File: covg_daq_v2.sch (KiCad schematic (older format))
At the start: 4 parts

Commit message: updates to README
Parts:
- added J?: HDMI_A, symbol Connector:HDMI_A
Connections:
- net labels added: GND
- wire segments 0 -> 12
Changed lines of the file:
@@
 L adc_dac_v1-eagle-import:MOUNT-HOLE3.0 H1
 U 1 1 60986F3F
-P 7450 7850
+P 9650 7550
 AR Path="/60986F3F" Ref="H1"  Part="1"
 AR Path="/6095A004/60986F3F" Ref="H?"  Part="1"
-F 0 "H1" H 7530 7873 59  0000 L BNN
-F 1 "MOUNT-HOLE3.0" H 7530 7753 59  0000 L BNN
-F 2 "adc_dac_v1:3,0" H 7450 7850 50  0001 C CNN
-F 3 "" H 7450 7850 50  0001 C CNN
-	1    7450 7850
+F 0 "H1" H 9730 7573 59  0000 L BNN
+F 1 "MOUNT-HOLE3.0" H 9730 7453 59  0000 L BNN
+F 2 "adc_dac_v1:3,0" H 9650 7550 50  0001 C CNN
+F 3 "" H 9650 7550 50  0001 C CNN
+	1    9650 7550
 	1    0    0    -1
 $EndComp
@@
 L adc_dac_v1-eagle-import:MOUNT-HOLE3.0 H2
 U 1 1 60986F45
-P 8550 7850
+P 10750 7550
 AR Path="/60986F45" Ref="H2"  Part="1"
 AR Path="/6095A004/60986F45" Ref="H?"  Part="1"
-F 0 "H2" H 8630 7873 59  0000 L BNN
-F 1 "MOUNT-HOLE3.0" H 8630 7753 59  0000 L BNN
-F 2 "adc_dac_v1:3,0" H 8550 7850 50  0001 C CNN
-F 3 "" H 8550 7850 50  0001 C CNN
-	1    8550 7850
+F 0 "H2" H 10830 7573 59  0000 L BNN
+F 1 "MOUNT-HOLE3.0" H 10830 7453 59  0000 L BNN
+F 2 "adc_dac_v1:3,0" H 10750 7550 50  0001 C CNN
+F 3 "" H 10750 7550 50  0001 C CNN
+	1    10750 7550
 	1    0    0    -1
 $EndComp
@@
 	1    0    0    -1
 $EndComp
+$Comp
+L Connector:HDMI_A J?
+U 1 1 61D74FD2
+P 1150 6550
+F 0 "J?" H 1580 6596 50  0000 L CNN
+F 1 "HDMI_A" H 1580 6505 50  0000 L CNN
+F 2 "" H 1175 6550 50  0001 C CNN
+F 3 "https://en.wikipedia.org/wiki/HDMI" H 1175 6550 50  0001 C CNN
+	1    1150 6550
+	-1   0    0    -1
+$EndComp
+$Comp
+L power:GND #PWR?
+U 1 1 61D76AA5
+P 700 7850
+F 0 "#PWR?" H 700 7600 50  0001 C CNN
+F 1 "GND" H 705 7677 50  0001 C CNN
+F 2 "" H 700 7850 50  0001 C CNN
+F 3 "" H 700 7850 50  0001 C CNN
+	1    700  7850
+	1    0    0    -1
+$EndComp
+Wire Wire Line
+	700  7850 850  7850
+Wire Wire Line
+	850  7850 850  7650
+Wire Wire Line
+	850  7850 950  7850
+Wire Wire Line
+	1350 7850 1350 7650
+Connection ~ 850  7850
+Wire Wire Line
+	1250 7650 1250 7850
+Connection ~ 1250 7850
+Wire Wire Line
+	1250 7850 1350 7850
+Wire Wire Line
+	1150 7850 1150 7650
+Connection ~ 1150 7850
+Wire Wire Line
+	1150 7850 1250 7850
+Wire Wire Line
+	1050 7650 1050 7850
+Connection ~ 1050 7850
+Wire Wire Line
+	1050 7850 1150 7850
+Wire Wire Line
+	950  7850 950  7650
+Connection ~ 950  7850
+Wire Wire Line
+	950  7850 1050 7850
 $EndSCHEMATC

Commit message: updates to fast adc schematic
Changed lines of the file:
@@
 $EndDescr
 $Sheet
-S 1000 1000 500  150
+S 8900 3600 500  150
 U 6095A004
 F0 "gp_adc" 50
@@
 $EndSheet
 $Sheet
-S 5000 1000 500  150
+S 7150 2200 500  150
 U 6095A38A
 F0 "level_shifters" 50
@@
 $EndSheet
 $Sheet
-S 7000 1000 500  150
+S 1400 4350 500  150
 U 6095A697
 F0 "adc1" 50
@@
 $EndSheet
 $Sheet
-S 5000 3000 500  150
+S 2450 4350 500  150
 U 6095B316
 F0 "dac1" 50
@@
 $EndSheet
 $Sheet
-S 3000 5000 500  150
+S 8900 950  500  150
 U 6095BD4C
 F0 "dac_gp" 50
@@
 $EndSheet
 $Sheet
-S 5000 5000 500  150
+S 8900 2300 500  150
 U 6095BE10
 F0 "power" 50
@@
 $EndSheet
 $Sheet
-S 3000 1000 500  150
+S 7200 900  500  150
 U 6095A302
 F0 "ok_fpga" 50

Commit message: completed fast ADC and DAC; start on gp DAC
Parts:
- removed H1, H2, H3, H4: MOUNT-HOLE3.0, adc_dac_v1:3,0, symbol adc_dac_v1-eagle-import:MOUNT-HOLE3.0
- added H? (x4): MountingHole_Pad, MountingHole:MountingHole_3.2mm_M3_DIN965_Pad, symbol Mechanical:MountingHole_Pad
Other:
- moved on the sheet: J?
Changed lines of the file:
@@
 $EndDescr
-$Sheet
-S 8900 3600 500  150
-U 6095A004
-F0 "gp_adc" 50
-F1 "gp_adc.sch" 50
-$EndSheet
 $Sheet
 S 7150 2200 500  150
@@
 F0 "level_shifters" 50
 F1 "level_shifters.sch" 50
-$EndSheet
-$Sheet
-S 1400 4350 500  150
-U 6095A697
-F0 "adc1" 50
-F1 "adc1.sch" 50
-$EndSheet
-$Sheet
-S 2450 4350 500  150
-U 6095B316
-F0 "dac1" 50
-F1 "dac1.sch" 50
 $EndSheet
 $Sheet
@@
 $EndSheet
 $Comp
-L adc_dac_v1-eagle-import:FRAME_A_L #FRAME2
-U 1 1 60986F39
-P 7050 8150
-AR Path="/60986F39" Ref="#FRAME2"  Part="1"
-AR Path="/6095A004/60986F39" Ref="#FRAME?"  Part="1"
-F 0 "#FRAME2" H 7050 8150 50  0001 C CNN
-F 1 "FRAME_A_L" H 7050 8150 50  0001 C CNN
-F 2 "" H 7050 8150 50  0001 C CNN
-F 3 "" H 7050 8150 50  0001 C CNN
-	1    7050 8150
+L Connector:HDMI_A J?
+U 1 1 61D74FD2
+P 2000 5950
+F 0 "J?" H 2430 5996 50  0000 L CNN
+F 1 "HDMI_A" H 2430 5905 50  0000 L CNN
+F 2 "" H 2025 5950 50  0001 C CNN
+F 3 "https://en.wikipedia.org/wiki/HDMI" H 2025 5950 50  0001 C CNN
+	1    2000 5950
+	0    -1   1    0
+$EndComp
+$Comp
+L power:GND #PWR0101
+U 1 1 61D76AA5
+P 3300 6400
+F 0 "#PWR0101" H 3300 6150 50  0001 C CNN
+F 1 "GND" H 3305 6227 50  0001 C CNN
+F 2 "" H 3300 6400 50  0001 C CNN
+F 3 "" H 3300 6400 50  0001 C CNN
+	1    3300 6400
+	0    -1   -1   0
+$EndComp
+Wire Wire Line
+	3300 6400 3300 6250
+Wire Wire Line
+	3300 6250 3100 6250
+Wire Wire Line
+	3300 6250 3300 6150
+Wire Wire Line
+	3300 5750 3100 5750
+Connection ~ 3300 6250
+Wire Wire Line
+	3100 5850 3300 5850
+Connection ~ 3300 5850
+Wire Wire Line
+	3300 5850 3300 5750
+Wire Wire Line
+	3300 5950 3100 5950
+Connection ~ 3300 5950
+Wire Wire Line
+	3300 5950 3300 5850
+Wire Wire Line
+	3100 6050 3300 6050
+Connection ~ 3300 6050
+Wire Wire Line
+	3300 6050 3300 5950
+Wire Wire Line
+	3300 6150 3100 6150
+Connection ~ 3300 6150
+Wire Wire Line
+	3300 6150 3300 6050
+$Sheet
+S 1000 3900 1050 950
+U 6095A697
+F0 "adc" 50
+F1 "adc.sch" 50
+F2 "CNV_P" I R 2050 3950 50
+F3 "CNV_N" I R 2050 4050 50
+F4 "D_N" O R 2050 4150 50
+F5 "DCO_N" O R 2050 4250 50
+F6 "DCO_P" O R 2050 4350 50
+F7 "CLK_N" I R 2050 4450 50
+F8 "CLK_P" I R 2050 4550 50
+F9 "VCM_OUT" O L 1000 4650 50
+F10 "IN_N" I L 1000 4200 50
+F11 "IN_P" I L 1000 4100 50
+F12 "A_EN0" I R 2050 4750 50
+$EndSheet
+$Sheet
+S 2850 3900 650  350
+U 6095B316
+F0 "dac" 50
+F1 "dac.sch" 50
+F2 "CSB" I L 2850 3950 50
+F3 "SCLK" I L 2850 4050 50
+F4 "SDI" I L 2850 4150 50
+F5 "OUT" O R 3500 4000 50
+$EndSheet
+$Comp
+L Mechanical:MountingHole_Pad H?
+U 1 1 60B0A4A6
+P 1700 750
+F 0 "H?" H 1800 799 50  0000 L CNN
+F 1 "MountingHole_Pad" H 1800 708 50  0000 L CNN
+F 2 "MountingHole:MountingHole_3.2mm_M3_DIN965_Pad" H 1700 750 50  0001 C CNN
+F 3 "~" H 1700 750 50  0001 C CNN
+	1    1700 750
 	1    0    0    -1
 $EndComp
 $Comp
-L adc_dac_v1-eagle-import:MOUNT-HOLE3.0 H1
-U 1 1 60986F3F
-P 9650 7550
-AR Path="/60986F3F" Ref="H1"  Part="1"
-AR Path="/6095A004/60986F3F" Ref="H?"  Part="1"
-F 0 "H1" H 9730 7573 59  0000 L BNN
-F 1 "MOUNT-HOLE3.0" H 9730 7453 59  0000 L BNN
-F 2 "adc_dac_v1:3,0" H 9650 7550 50  0001 C CNN
-F 3 "" H 9650 7550 50  0001 C CNN
-	1    9650 7550
+L Mechanical:MountingHole_Pad H?
+U 1 1 60B0AC43
+P 700 750
+F 0 "H?" H 800 799 50  0000 L CNN
+F 1 "MountingHole_Pad" H 800 708 50  0000 L CNN
+F 2 "MountingHole:MountingHole_3.2mm_M3_DIN965_Pad" H 700 750 50  0001 C CNN
+F 3 "~" H 700 750 50  0001 C CNN
+	1    700  750
 	1    0    0    -1
 $EndComp
 $Comp
-L adc_dac_v1-eagle-import:MOUNT-HOLE3.0 H2
-U 1 1 60986F45
-P 10750 7550
-AR Path="/60986F45" Ref="H2"  Part="1"
-AR Path="/6095A004/60986F45" Ref="H?"  Part="1"
-F 0 "H2" H 10830 7573 59  0000 L BNN
-F 1 "MOUNT-HOLE3.0" H 10830 7453 59  0000 L BNN
-F 2 "adc_dac_v1:3,0" H 10750 7550 50  0001 C CNN
-F 3 "" H 10750 7550 50  0001 C CNN
-	1    10750 7550
+L Mechanical:MountingHole_Pad H?
+U 1 1 60B0ADFD
+P 700 1200
+F 0 "H?" H 800 1249 50  0000 L CNN
+F 1 "MountingHole_Pad" H 800 1158 50  0000 L CNN
+F 2 "MountingHole:MountingHole_3.2mm_M3_DIN965_Pad" H 700 1200 50  0001 C CNN
+F 3 "~" H 700 1200 50  0001 C CNN
+	1    700  1200
 	1    0    0    -1
 $EndComp
 $Comp
-L adc_dac_v1-eagle-import:MOUNT-HOLE3.0 H3
-U 1 1 60986F4B
-P 9650 7850
-AR Path="/60986F4B" Ref="H3"  Part="1"
-AR Path="/6095A004/60986F4B" Ref="H?"  Part="1"
-F 0 "H3" H 9730 7873 59  0000 L BNN
-F 1 "MOUNT-HOLE3.0" H 9730 7753 59  0000 L BNN
-F 2 "adc_dac_v1:3,0" H 9650 7850 50  0001 C CNN
-F 3 "" H 9650 7850 50  0001 C CNN
-	1    9650 7850
+L Mechanical:MountingHole_Pad H?
+U 1 1 60B0B098
+P 1700 1200
+F 0 "H?" H 1800 1249 50  0000 L CNN
+F 1 "MountingHole_Pad" H 1800 1158 50  0000 L CNN
+F 2 "MountingHole:MountingHole_3.2mm_M3_DIN965_Pad" H 1700 1200 50  0001 C CNN
+F 3 "~" H 1700 1200 50  0001 C CNN
+	1    1700 1200
 	1    0    0    -1
 $EndComp
-$Comp
-L adc_dac_v1-eagle-import:MOUNT-HOLE3.0 H4
-U 1 1 60986F51
-P 10750 7850
-AR Path="/60986F51" Ref="H4"  Part="1"
-AR Path="/6095A004/60986F51" Ref="H?"  Part="1"
-F 0 "H4" H 10830 7873 59  0000 L BNN
-F 1 "MOUNT-HOLE3.0" H 10830 7753 59  0000 L BNN
-F 2 "adc_dac_v1:3,0" H 10750 7850 50  0001 C CNN
-F 3 "" H 10750 7850 50  0001 C CNN
-	1    10750 7850
-	1    0    0    -1
-$EndComp
-$Comp
-L Connector:HDMI_A J?
-U 1 1 61D74FD2
-P 1150 6550
-F 0 "J?" H 1580 6596 50  0000 L CNN
-F 1 "HDMI_A" H 1580 6505 50  0000 L CNN
-F 2 "" H 1175 6550 50  0001 C CNN
-F 3 "https://en.wikipedia.org/wiki/HDMI" H 1175 6550 50  0001 C CNN
-	1    1150 6550
-	-1   0    0    -1
-$EndComp
-$Comp
-L power:GND #PWR?
-U 1 1 61D76AA5
-P 700 7850
-F 0 "#PWR?" H 700 7600 50  0001 C CNN
-F 1 "GND" H 705 7677 50  0001 C CNN
-F 2 "" H 700 7850 50  0001 C CNN
-F 3 "" H 700 7850 50  0001 C CNN
-	1    700  7850
-	1    0    0    -1
-$EndComp
-Wire Wire Line
-	700  7850 850  7850
-Wire Wire Line
-	850  7850 850  7650
-Wire Wire Line
-	850  7850 950  7850
-Wire Wire Line
-	1350 7850 1350 7650
-Connection ~ 850  7850
-Wire Wire Line
-	1250 7650 1250 7850
-Connection ~ 1250 7850
-Wire Wire Line
-	1250 7850 1350 7850
-Wire Wire Line
-	1150 7850 1150 7650
-Connection ~ 1150 7850
-Wire Wire Line
-	1150 7850 1250 7850
-Wire Wire Line
-	1050 7650 1050 7850
-Connection ~ 1050 7850
-Wire Wire Line
-	1050 7850 1150 7850
-Wire Wire Line
-	950  7850 950  7650
-Connection ~ 950  7850
-Wire Wire Line
-	950  7850 1050 7850
+$Sheet
+S 8900 3600 500  150
+U 6095A004
+F0 "adc_gp" 50
+F1 "adc_gp.sch" 50
+$EndSheet
 $EndSCHEMATC

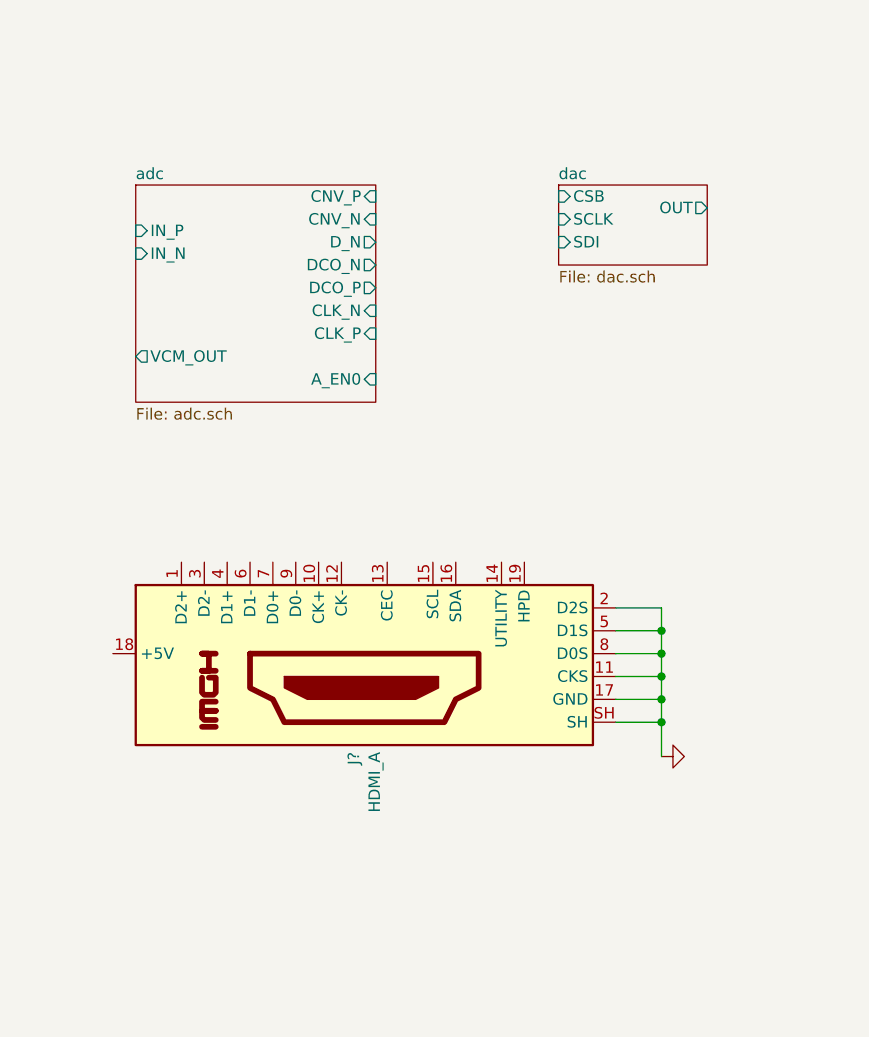
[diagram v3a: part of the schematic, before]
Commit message: updates to the gp DAC
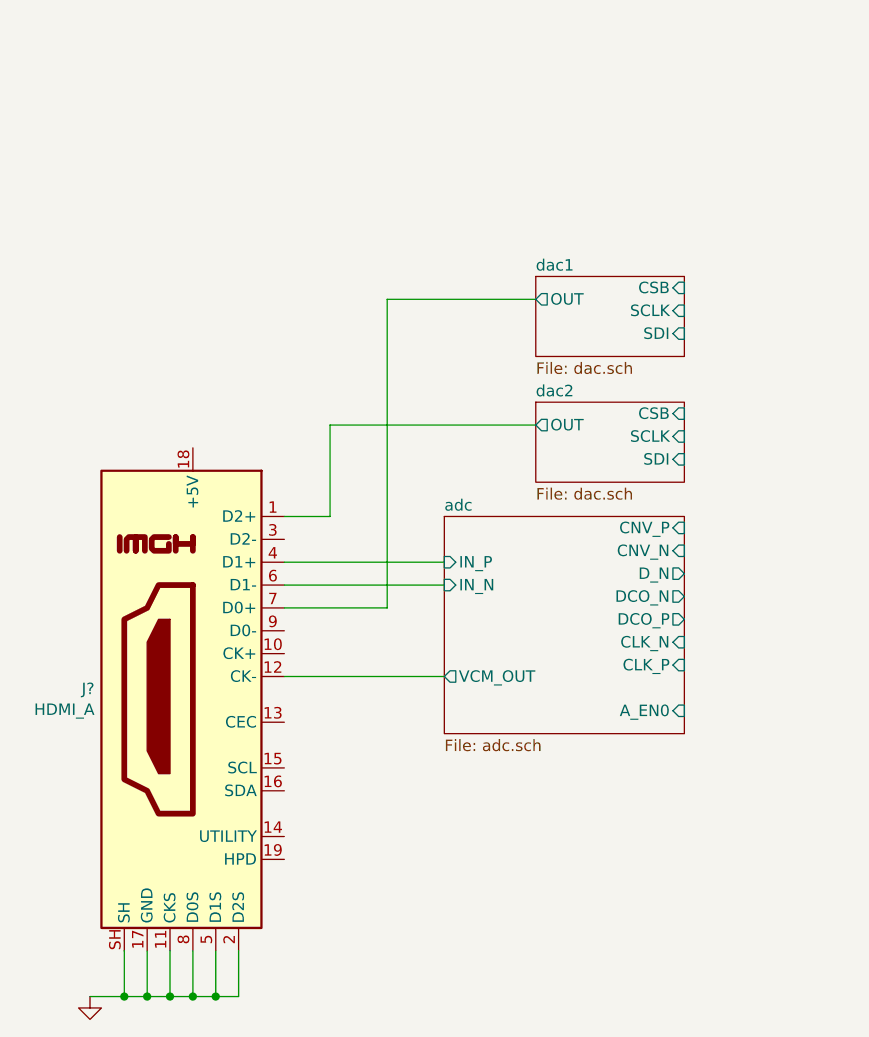
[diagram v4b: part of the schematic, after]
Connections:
- net adc/IN_N: now also J?.6 (D1-)
- net adc/IN_P: now also J?.4 (D1+)
- net adc/VCM_OUT: now also J?.12 (CK-)
- net dac2/OUT: now reaches J?.1 (D2+)
- net dac1/OUT: now reaches J?.7 (D0+)
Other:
- moved on the sheet: J?
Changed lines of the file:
@@
 $Descr A4 11693 8268
 encoding utf-8
-Sheet 1 8
+Sheet 1 9
 Title ""
 Date ""
@@
 L Connector:HDMI_A J?
 U 1 1 61D74FD2
-P 2000 5950
-F 0 "J?" H 2430 5996 50  0000 L CNN
-F 1 "HDMI_A" H 2430 5905 50  0000 L CNN
-F 2 "" H 2025 5950 50  0001 C CNN
-F 3 "https://en.wikipedia.org/wiki/HDMI" H 2025 5950 50  0001 C CNN
-	1    2000 5950
-	0    -1   1    0
+P 1250 6150
+F 0 "J?" H 1680 6196 50  0000 L CNN
+F 1 "HDMI_A" H 1680 6105 50  0000 L CNN
+F 2 "" H 1275 6150 50  0001 C CNN
+F 3 "https://en.wikipedia.org/wiki/HDMI" H 1275 6150 50  0001 C CNN
+	1    1250 6150
+	-1   0    0    -1
 $EndComp
 $Comp
 L power:GND #PWR0101
 U 1 1 61D76AA5
-P 3300 6400
-F 0 "#PWR0101" H 3300 6150 50  0001 C CNN
-F 1 "GND" H 3305 6227 50  0001 C CNN
-F 2 "" H 3300 6400 50  0001 C CNN
-F 3 "" H 3300 6400 50  0001 C CNN
-	1    3300 6400
-	0    -1   -1   0
+P 800 7450
+F 0 "#PWR0101" H 800 7200 50  0001 C CNN
+F 1 "GND" H 805 7277 50  0001 C CNN
+F 2 "" H 800 7450 50  0001 C CNN
+F 3 "" H 800 7450 50  0001 C CNN
+	1    800  7450
+	1    0    0    -1
 $EndComp
 Wire Wire Line
-	3300 6400 3300 6250
+	800  7450 950  7450
 Wire Wire Line
-	3300 6250 3100 6250
+	950  7450 950  7250
 Wire Wire Line
-	3300 6250 3300 6150
+	950  7450 1050 7450
 Wire Wire Line
-	3300 5750 3100 5750
-Connection ~ 3300 6250
+	1450 7450 1450 7250
+Connection ~ 950  7450
 Wire Wire Line
-	3100 5850 3300 5850
-Connection ~ 3300 5850
+	1350 7250 1350 7450
+Connection ~ 1350 7450
 Wire Wire Line
-	3300 5850 3300 5750
+	1350 7450 1450 7450
 Wire Wire Line
-	3300 5950 3100 5950
-Connection ~ 3300 5950
+	1250 7450 1250 7250
+Connection ~ 1250 7450
 Wire Wire Line
-	3300 5950 3300 5850
+	1250 7450 1350 7450
 Wire Wire Line
-	3100 6050 3300 6050
-Connection ~ 3300 6050
+	1150 7250 1150 7450
+Connection ~ 1150 7450
 Wire Wire Line
-	3300 6050 3300 5950
+	1150 7450 1250 7450
 Wire Wire Line
-	3300 6150 3100 6150
-Connection ~ 3300 6150
+	1050 7450 1050 7250
+Connection ~ 1050 7450
 Wire Wire Line
-	3300 6150 3300 6050
+	1050 7450 1150 7450
 $Sheet
-S 1000 3900 1050 950
+S 2350 5350 1050 950
 U 6095A697
 F0 "adc" 50
 F1 "adc.sch" 50
-F2 "CNV_P" I R 2050 3950 50
-F3 "CNV_N" I R 2050 4050 50
-F4 "D_N" O R 2050 4150 50
-F5 "DCO_N" O R 2050 4250 50
-F6 "DCO_P" O R 2050 4350 50
-F7 "CLK_N" I R 2050 4450 50
-F8 "CLK_P" I R 2050 4550 50
-F9 "VCM_OUT" O L 1000 4650 50
-F10 "IN_N" I L 1000 4200 50
-F11 "IN_P" I L 1000 4100 50
-F12 "A_EN0" I R 2050 4750 50
+F2 "CNV_P" I R 3400 5400 50
+F3 "CNV_N" I R 3400 5500 50
+F4 "D_N" O R 3400 5600 50
+F5 "DCO_N" O R 3400 5700 50
+F6 "DCO_P" O R 3400 5800 50
+F7 "CLK_N" I R 3400 5900 50
+F8 "CLK_P" I R 3400 6000 50
+F9 "VCM_OUT" O L 2350 6050 50
+F10 "IN_N" I L 2350 5650 50
+F11 "IN_P" I L 2350 5550 50
+F12 "A_EN0" I R 3400 6200 50
 $EndSheet
 $Sheet
-S 2850 3900 650  350
+S 2750 4300 650  350
 U 6095B316
-F0 "dac" 50
+F0 "dac1" 50
 F1 "dac.sch" 50
-F2 "CSB" I L 2850 3950 50
-F3 "SCLK" I L 2850 4050 50
-F4 "SDI" I L 2850 4150 50
-F5 "OUT" O R 3500 4000 50
+F2 "CSB" I R 3400 4350 50
+F3 "SCLK" I R 3400 4450 50
+F4 "SDI" I R 3400 4550 50
+F5 "OUT" O L 2750 4400 50
 $EndSheet
 $Comp
@@
 F1 "adc_gp.sch" 50
 $EndSheet
+Wire Wire Line
+	1650 5550 2350 5550
+Wire Wire Line
+	2350 5650 1650 5650
+Wire Wire Line
+	2350 6050 1650 6050
+$Sheet
+S 2750 4850 650  350
+U 60BDA97E
+F0 "dac2" 50
+F1 "dac.sch" 50
+F2 "CSB" I R 3400 4900 50
+F3 "SCLK" I R 3400 5000 50
+F4 "SDI" I R 3400 5100 50
+F5 "OUT" O L 2750 4950 50
+$EndSheet
+Wire Wire Line
+	1650 5350 1850 5350
+Wire Wire Line
+	1850 5350 1850 4950
+Wire Wire Line
+	1850 4950 2750 4950
+Wire Wire Line
+	2100 5750 2100 4400
+Wire Wire Line
+	2100 4400 2750 4400
+Wire Wire Line
+	1650 5750 2100 5750
 $EndSCHEMATC

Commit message: updates to gp_dac
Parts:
- gave numbers to parts that had none: 5
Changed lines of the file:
@@
 $Descr A4 11693 8268
 encoding utf-8
-Sheet 1 9
+Sheet 1 10
 Title ""
 Date ""
@@
 $EndSheet
 $Comp
-L Connector:HDMI_A J?
+L Connector:HDMI_A J3
 U 1 1 61D74FD2
 P 1250 6150
-F 0 "J?" H 1680 6196 50  0000 L CNN
+F 0 "J3" H 1680 6196 50  0000 L CNN
 F 1 "HDMI_A" H 1680 6105 50  0000 L CNN
 F 2 "" H 1275 6150 50  0001 C CNN
@@
 $EndSheet
 $Comp
-L Mechanical:MountingHole_Pad H?
+L Mechanical:MountingHole_Pad H3
 U 1 1 60B0A4A6
 P 1700 750
-F 0 "H?" H 1800 799 50  0000 L CNN
+F 0 "H3" H 1800 799 50  0000 L CNN
 F 1 "MountingHole_Pad" H 1800 708 50  0000 L CNN
 F 2 "MountingHole:MountingHole_3.2mm_M3_DIN965_Pad" H 1700 750 50  0001 C CNN
@@
 $EndComp
 $Comp
-L Mechanical:MountingHole_Pad H?
+L Mechanical:MountingHole_Pad H1
 U 1 1 60B0AC43
 P 700 750
-F 0 "H?" H 800 799 50  0000 L CNN
+F 0 "H1" H 800 799 50  0000 L CNN
 F 1 "MountingHole_Pad" H 800 708 50  0000 L CNN
 F 2 "MountingHole:MountingHole_3.2mm_M3_DIN965_Pad" H 700 750 50  0001 C CNN
@@
 $EndComp
 $Comp
-L Mechanical:MountingHole_Pad H?
+L Mechanical:MountingHole_Pad H2
 U 1 1 60B0ADFD
 P 700 1200
-F 0 "H?" H 800 1249 50  0000 L CNN
+F 0 "H2" H 800 1249 50  0000 L CNN
 F 1 "MountingHole_Pad" H 800 1158 50  0000 L CNN
 F 2 "MountingHole:MountingHole_3.2mm_M3_DIN965_Pad" H 700 1200 50  0001 C CNN
@@
 $EndComp
 $Comp
-L Mechanical:MountingHole_Pad H?
+L Mechanical:MountingHole_Pad H4
 U 1 1 60B0B098
 P 1700 1200
-F 0 "H?" H 1800 1249 50  0000 L CNN
+F 0 "H4" H 1800 1249 50  0000 L CNN
 F 1 "MountingHole_Pad" H 1800 1158 50  0000 L CNN
 F 2 "MountingHole:MountingHole_3.2mm_M3_DIN965_Pad" H 1700 1200 50  0001 C CNN

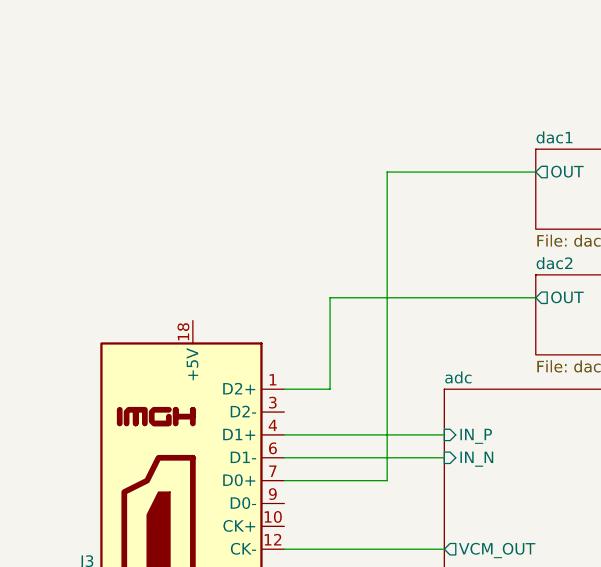
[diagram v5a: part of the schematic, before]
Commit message: completed gp adc
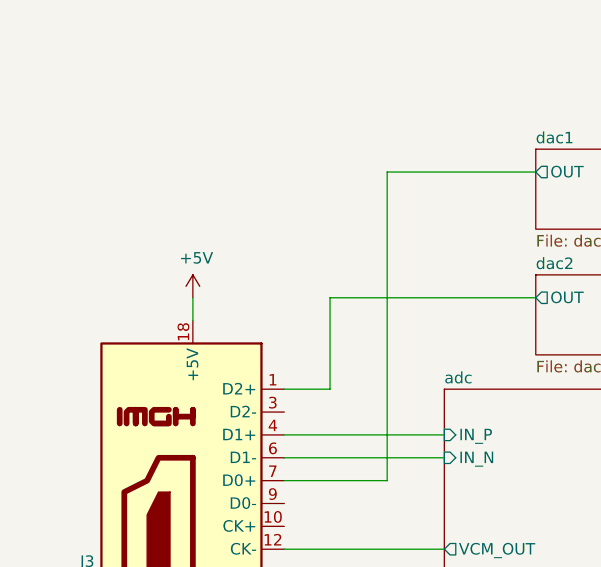
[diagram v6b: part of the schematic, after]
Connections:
- net +5V: now reaches J3.18 (+5V)
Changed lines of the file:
@@
 Wire Wire Line
 	1650 5750 2100 5750
+$Comp
+L power:+5V #PWR?
+U 1 1 628A3CF1
+P 1250 4950
+F 0 "#PWR?" H 1250 4800 50  0001 C CNN
+F 1 "+5V" H 1265 5123 50  0000 C CNN
+F 2 "" H 1250 4950 50  0001 C CNN
+F 3 "" H 1250 4950 50  0001 C CNN
+	1    1250 4950
+	1    0    0    -1
+$EndComp
+Wire Wire Line
+	1250 4950 1250 5050
 $EndSCHEMATC
